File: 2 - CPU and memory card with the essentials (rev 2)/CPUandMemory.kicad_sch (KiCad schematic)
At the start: 8 parts, among them U10 AS6C4008, U11 AS6C4008, U8 Z84C0010, U9 SST39SF010

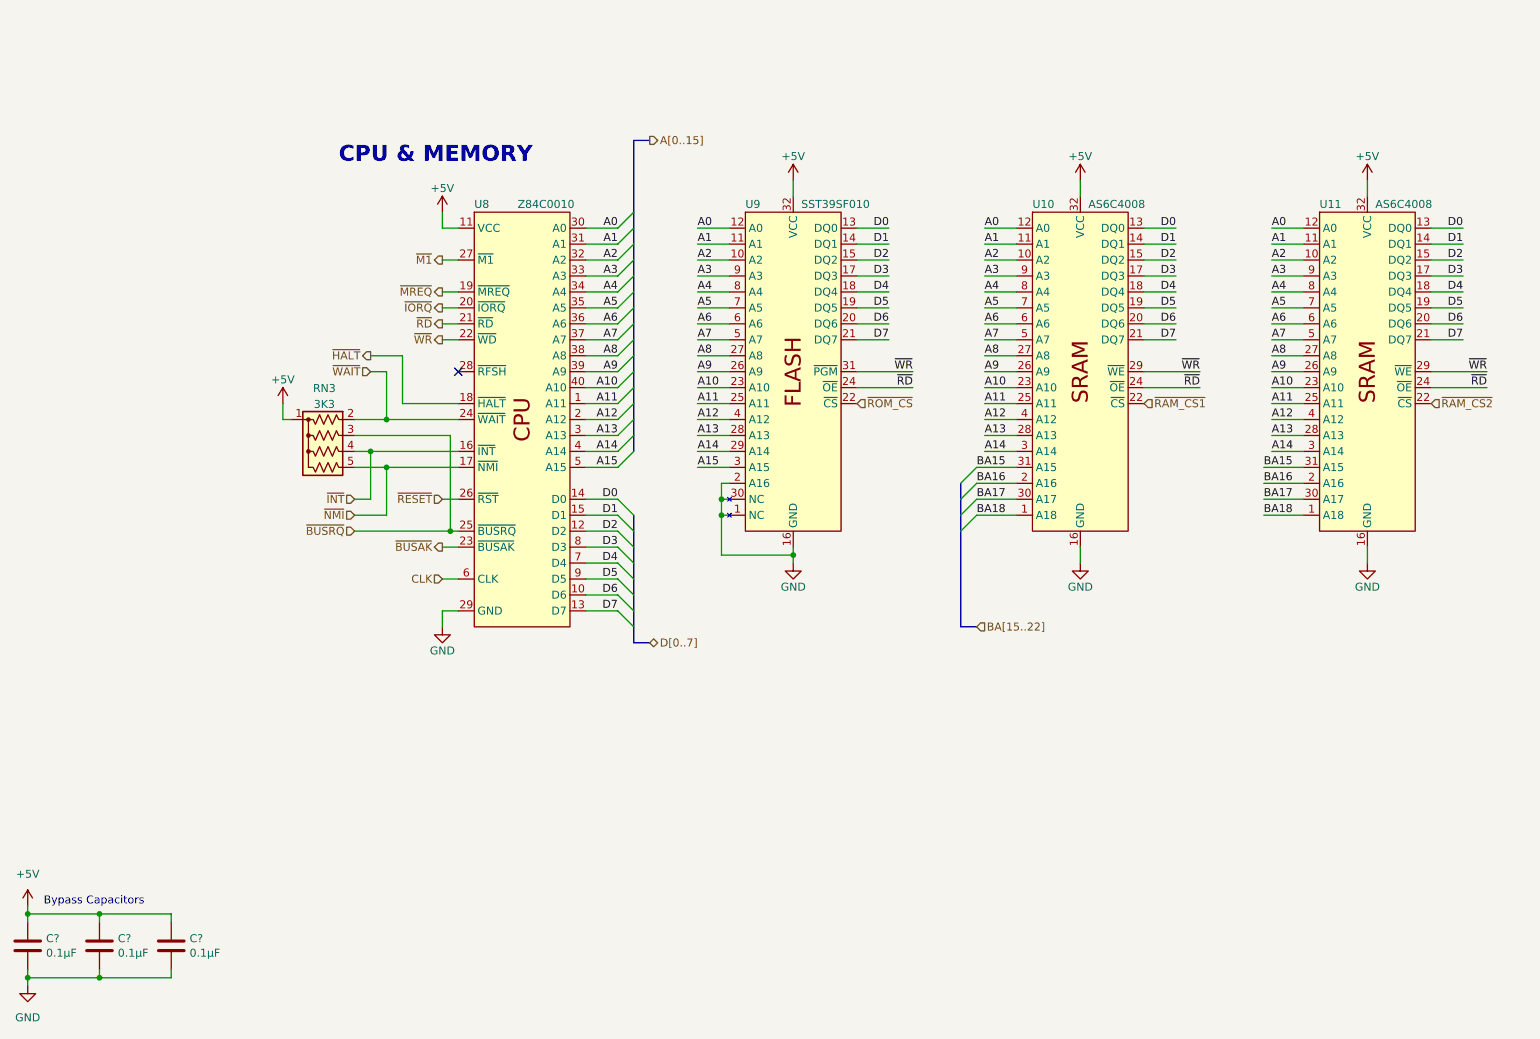
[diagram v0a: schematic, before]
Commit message: Updated disk activity circuit in mother board, and improved layout in CPU card
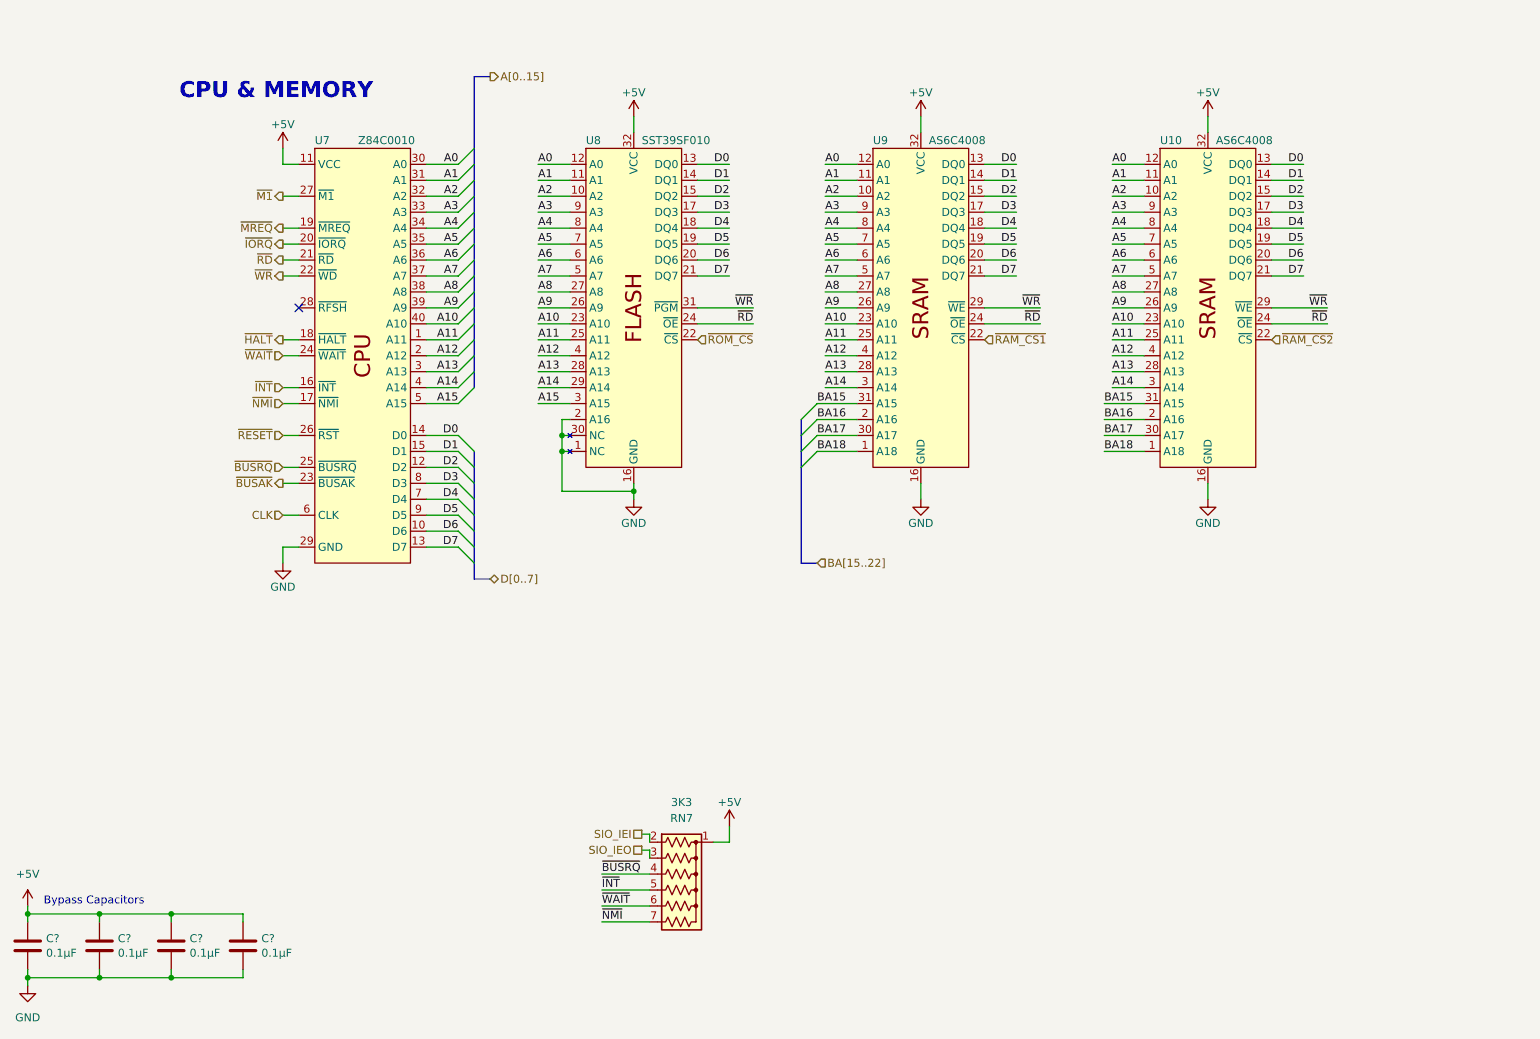
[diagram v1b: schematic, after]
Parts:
- removed RN3: 3K3, Resistor_THT:R_Array_SIP5, symbol Device:R_Network04_US
- added C?: 0.1µF, Capacitor_THT:C_Disc_D3.0mm_W1.6mm_P2.50mm, symbol Device:C
- added RN7: 3K3, Resistor_THT:R_Array_SIP7, symbol Device:R_Network06_US
- U8: renamed from U9; footprint Socket:DIP_Socket-32_W11.9_W12.7_W15.24_W17.78_W18.5_3M_232-1285-00-0602J -> 0_Library:DIP_Socket-32_W11.9_W12.7_W15.24_W17.78_W18.5_3M_232-1285-00-0602J
- renumbered U11 to U10, U8 to U7, U10 to U9
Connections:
- net +5V: now also C?.1, RN7.1 (common)
- net GND: now also C?.2
- net ~{BUSRQ}: now also RN7.4 (R3)
- net ~{INT}: now also RN7.5 (R4)
- net ~{NMI}: now also RN7.7 (R6)
- net ~{WAIT}: now also RN7.6 (R5)
- new net SIO_IEI: RN7.2 (R1)
- new net SIO_IEO: RN7.3 (R2)
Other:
- moved on the sheet: U10, U7, U8, U9

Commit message: Trying to hash out the flaws
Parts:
- removed C?: 0.1µF, Capacitor_THT:C_Disc_D3.0mm_W1.6mm_P2.50mm, symbol Device:C
- removed U10: AS6C4008, Package_DIP:DIP-32_W15.24mm_Socket, symbol 0_Library:AS6C4008
- added BAR1: STATUS, 0_Library:BAR_GRAPH_8, symbol 0_Library:BAR_GRAPH_8
- added C?: 0.1µF, Capacitor_THT:C_Disc_D3.0mm_W1.6mm_P2.50mm, symbol Device:C
- added RN3: 300, Resistor_THT:R_Array_SIP9, symbol Device:R_Network08_US
- added SW1: PAGE, 0_Library:Microswitch_2.54mm_spacing, symbol Switch:SW_SPDT
- added U16: 74HCT563, Package_DIP:DIP-20_W7.62mm_Socket, symbol 0_Library:74HC563
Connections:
- net ~{RAM_CS1} is gone; now on net ~{MREQ}: U9.22 (~{CS})
- net +5V: now also C?.1, SW1.1 (A), U16.20 (VCC)
- net GND: now also C?.2, RN3.1 (common), SW1.3 (C), U16.1 (OE), U16.10 (GND); no longer U8.2 (A16)
- net ~{BUSAK}: now also U16.5 (D3)
- net ~{BUSRQ}: now also U16.4 (D2)
- net ~{HALT}: now also U16.6 (D4)
- net ~{INT}: now also U16.8 (D6)
- net ~{NMI}: now also U16.9 (D7)
- net ~{RD}: no longer U9.24 (~{OE})
- net ~{RESET}: now also U16.2 (D0)
- net ~{ROM_CS}: now also U16.3 (D1)
- net ~{WAIT}: now also U16.7 (D5)
- new net: SW1.2 (B), U8.2 (A16)
- new net: BAR1.10 (A), RN3.8 (R7)
- new net: BAR1.11 (K), RN3.7 (R6)
- new net: BAR1.12 (K), RN3.6 (R5)
- new net: BAR1.13 (K), RN3.5 (R4)
- new net: BAR1.14 (K), RN3.4 (R3)
- new net: BAR1.15 (K), RN3.3 (R2)
- new net: BAR1.16 (K), RN3.2 (R1)
- new net: BAR1.9 (A), RN3.9 (R8)
- new net BUSAK: BAR1.4 (A), U16.16 (Q3)
- new net BUSRQ: BAR1.3 (A), U16.17 (Q2)
- new net CLK2: U16.11 (LE)
- new net HALT: BAR1.5 (A), U16.15 (Q4)
- new net INT: BAR1.7 (A), U16.13 (Q6)
- new net NMI: BAR1.8 (A), U16.12 (Q7)
- new net RESET: BAR1.1 (A), U16.19 (Q0)
- new net SHADOW: BAR1.2 (A), U16.18 (Q1)
- new net WAIT: BAR1.6 (A), U16.14 (Q5)
- new net ~{RAM_OE}: U9.24 (~{OE})
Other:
- note added: "BLINKENLIGHTS"
- moved on the sheet: RN7, U7, U8, U9
